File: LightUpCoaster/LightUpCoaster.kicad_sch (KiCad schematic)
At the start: 24 parts, among them Q101 2N7002, Q102 BSS84, SW102 SW_SPDT, SW103 SW_DIP_x01, U103 CR2032, U104 NE555D, U105 4017

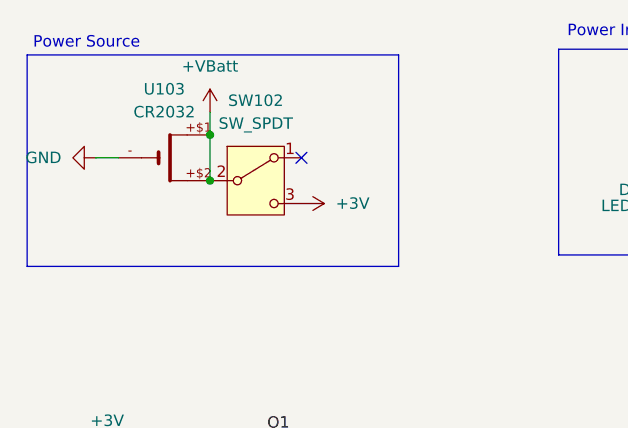
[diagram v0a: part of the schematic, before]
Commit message: Fixed LED positions
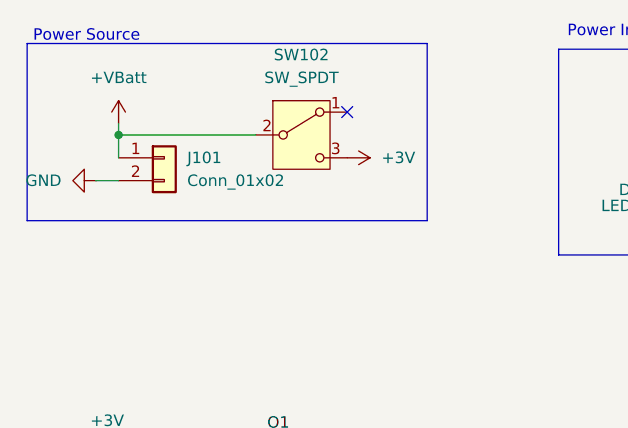
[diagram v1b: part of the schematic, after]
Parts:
- removed U103: CR2032, Battery_Holder:CR2032-SMD, symbol CR2032:CR2032
- added J101: Conn_01x02, Connector_PinHeader_2.54mm:PinHeader_1x02_P2.54mm_Vertical, symbol Connector_Generic:Conn_01x02
- SW103: footprint Button_Switch_SMD:SW_Push_1P1T_XKB_TS-1187A -> Button_Switch_SMD:SW_Push_1P1T_NO_E-Switch_TL3301NxxxxxG
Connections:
- net +VBatt: now also J101.1 (Pin_1)
- net GND: now also J101.2 (Pin_2)
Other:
- moved on the sheet: SW102
